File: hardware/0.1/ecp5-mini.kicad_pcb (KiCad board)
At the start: 4 copper layers, 52 x 27 mm, 109 parts, among them J1 Micro_SD_Card, J2 JTAG, J3 S7 Mini, J4 S7 Mini, J5 USB_C_Receptacle_USB2.0, Q1 BSS138, Q2 BSS138, Q3 BSS138, Q4 BSS138, SW1 SW_Push, U1 ECP5U_12_CABGA256, U2 TLV73325PDBV, U3 TLV62568DBV, U4 USBLC6-2SC6, U5 TLV62568DBV, U6 W25Q128JVSIQ, U7 S27KL0641

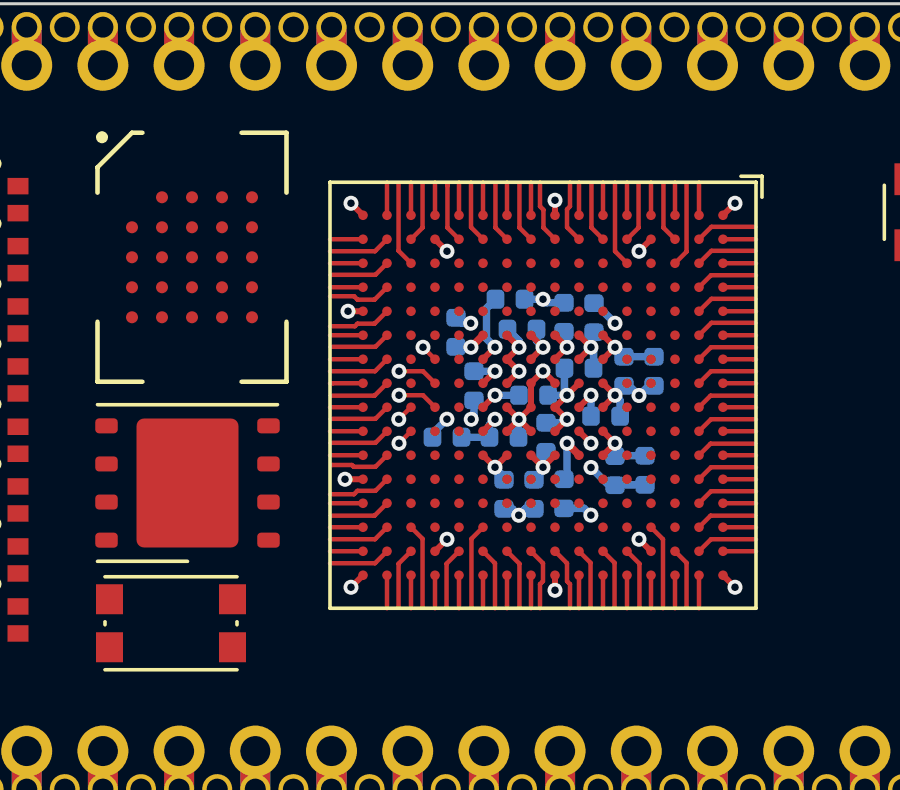
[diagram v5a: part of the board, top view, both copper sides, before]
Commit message: cleaning up schematic
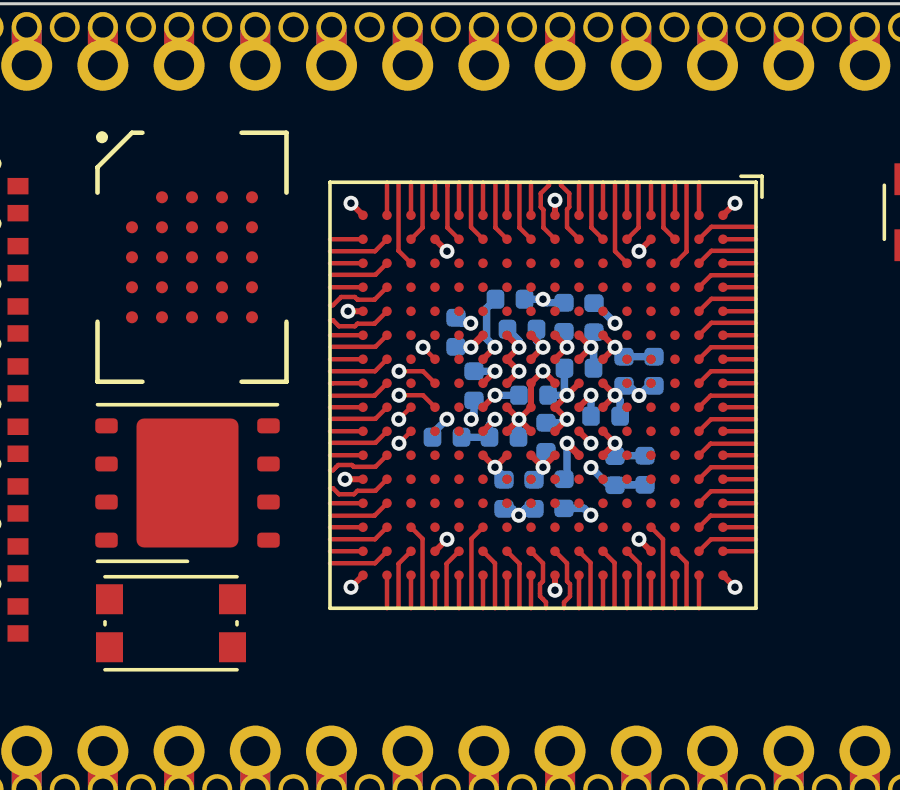
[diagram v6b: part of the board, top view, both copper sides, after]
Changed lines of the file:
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@@
   (segment (start 117.6 92.9) (end 117.115 92.9) (width 0.25) (layer "B.Cu") (net 100))
   (segment (start 118.4 96.9) (end 118.4 96.915) (width 0.25) (layer "B.Cu") (net 100))
-  (segment (start 113.628001 96.824999) (end 112.975001 96.824999) (width 0.15) (layer "F.Cu") (net 102))
+  (segment (start 113.175001 96.824999) (end 113.1 96.9) (width 0.15) (layer "F.Cu") (net 102))
   (segment (start 114.414999 96.885001) (end 113.688003 96.885001) (width 0.15) (layer "F.Cu") (net 102))
-  (segment (start 112.975001 96.824999) (end 112.924999 96.824999) (width 0.15) (layer "F.Cu") (net 102))
+  (segment (start 113.1 96.9) (end 113 97) (width 0.15) (layer "F.Cu") (net 102))
+  (segment (start 113 97) (end 112.9 97) (width 0.15) (layer "F.Cu") (net 102))
   (segment (start 114.8 96.5) (end 114.414999 96.885001) (width 0.15) (layer "F.Cu") (net 102))
   (segment (start 113.688003 96.885001) (end 113.628001 96.824999) (width 0.15) (layer "F.Cu") (net 102))
+  (segment (start 113.628001 96.824999) (end 113.175001 96.824999) (width 0.15) (layer "F.Cu") (net 102))
   (segment (start 114 95.7) (end 112.9 95.7) (width 0.15) (layer "F.Cu") (net 104))
   (segment (start 114.8 100.5) (end 114.8 101.6) (width 0.15) (layer "F.Cu") (net 106))
@@
   (segment (start 118.8 99.7) (end 119.214999 100.114999) (width 0.15) (layer "F.Cu") (net 124))
   (segment (start 119.214999 100.114999) (end 119.214999 101.585001) (width 0.15) (layer "F.Cu") (net 124))
+  (segment (start 120.1 101.4) (end 120.1 101.6) (width 0.15) (layer "F.Cu") (net 125))
+  (segment (start 120 101.3) (end 120.1 101.4) (width 0.15) (layer "F.Cu") (net 125))
   (segment (start 120 100.1) (end 120 100.696998) (width 0.15) (layer "F.Cu") (net 125))
+  (segment (start 119.9 101.2) (end 119.9 101.1) (width 0.15) (layer "F.Cu") (net 125))
   (segment (start 120 100.696998) (end 119.9 100.796998) (width 0.15) (layer "F.Cu") (net 125))
   (segment (start 119.6 99.7) (end 120 100.1) (width 0.15) (layer "F.Cu") (net 125))
-  (segment (start 119.9 100.796998) (end 119.9 101.6) (width 0.15) (layer "F.Cu") (net 125))
+  (segment (start 119.9 100.796998) (end 119.9 101.1) (width 0.15) (layer "F.Cu") (net 125))
+  (segment (start 120 101.3) (end 119.9 101.2) (width 0.15) (layer "F.Cu") (net 125))
+  (segment (start 120.9 100.796998) (end 120.9 101.1) (width 0.15) (layer "F.Cu") (net 126))
   (segment (start 120.8 100.1) (end 120.8 100.696998) (width 0.15) (layer "F.Cu") (net 126))
   (segment (start 120.4 99.7) (end 120.8 100.1) (width 0.15) (layer "F.Cu") (net 126))
+  (segment (start 120.7 101.403002) (end 120.7 101.6) (width 0.15) (layer "F.Cu") (net 126))
   (segment (start 120.8 100.696998) (end 120.9 100.796998) (width 0.15) (layer "F.Cu") (net 126))
-  (segment (start 120.9 100.796998) (end 120.9 101.6) (width 0.15) (layer "F.Cu") (net 126))
+  (segment (start 120.9 101.1) (end 120.9 101.203002) (width 0.15) (layer "F.Cu") (net 126))
+  (segment (start 120.9 101.203002) (end 120.7 101.403002) (width 0.15) (layer "F.Cu") (net 126))
   (segment (start 121.2 99.7) (end 121.585001 100.085001) (width 0.15) (layer "F.Cu") (net 127))
   (segment (start 121.585001 100.085001) (end 121.585001 101.585001) (width 0.15) (layer "F.Cu") (net 127))
@@
   (segment (start 125.6 97.7) (end 127.1 97.7) (width 0.15) (layer "F.Cu") (net 163))
   (segment (start 126 98.1) (end 127.1 98.1) (width 0.15) (layer "F.Cu") (net 164))
-  (segment (start 113.7 97.8) (end 112.9 97.8) (width 0.15) (layer "F.Cu") (net 165))
   (segment (start 114.8 97.3) (end 114.414999 97.685001) (width 0.15) (layer "F.Cu") (net 165))
+  (segment (start 113.7 97.8) (end 113.2 97.8) (width 0.15) (layer "F.Cu") (net 165))
+  (segment (start 113.2 97.8) (end 113 97.6) (width 0.15) (layer "F.Cu") (net 165))
   (segment (start 114.414999 97.685001) (end 113.814999 97.685001) (width 0.15) (layer "F.Cu") (net 165))
+  (segment (start 113 97.6) (end 112.9 97.6) (width 0.15) (layer "F.Cu") (net 165))
   (segment (start 113.814999 97.685001) (end 113.7 97.8) (width 0.15) (layer "F.Cu") (net 165))
   (segment (start 125.2 97.3) (end 125.6 96.9) (width 0.15) (layer "F.Cu") (net 178))
@@
   (segment (start 113 94.1) (end 112.9 94.1) (width 0.15) (layer "F.Cu") (net 228))
   (segment (start 114 94.1) (end 113 94.1) (width 0.15) (layer "F.Cu") (net 228))
+  (segment (start 113.2 92.2) (end 113 92) (width 0.15) (layer "F.Cu") (net 238))
   (segment (start 114.385001 92.114999) (end 113.815199 92.114999) (width 0.15) (layer "F.Cu") (net 238))
-  (segment (start 113.730198 92.2) (end 112.9 92.2) (width 0.15) (layer "F.Cu") (net 238))
+  (segment (start 113 92) (end 112.9 92) (width 0.15) (layer "F.Cu") (net 238))
+  (segment (start 113.730198 92.2) (end 113.2 92.2) (width 0.15) (layer "F.Cu") (net 238))
   (segment (start 113.815199 92.114999) (end 113.730198 92.2) (width 0.15) (layer "F.Cu") (net 238))
   (segment (start 114.8 91.7) (end 114.385001 92.114999) (width 0.15) (layer "F.Cu") (net 238))
   (segment (start 114 90.9) (end 112.9 90.9) (width 0.15) (layer "F.Cu") (net 248))
-  (segment (start 113.818001 91.314999) (end 113.703002 91.2) (width 0.15) (layer "F.Cu") (net 249))
-  (segment (start 113.703002 91.2) (end 112.9 91.2) (width 0.15) (layer "F.Cu") (net 249))
   (segment (start 114.8 90.9) (end 114.385001 91.314999) (width 0.15) (layer "F.Cu") (net 249))
+  (segment (start 113.271999 91.224999) (end 112.996998 91.5) (width 0.15) (layer "F.Cu") (net 249))
+  (segment (start 113.728001 91.224999) (end 113.271999 91.224999) (width 0.15) (layer "F.Cu") (net 249))
   (segment (start 114.385001 91.314999) (end 113.818001 91.314999) (width 0.15) (layer "F.Cu") (net 249))
+  (segment (start 113.818001 91.314999) (end 113.728001 91.224999) (width 0.15) (layer "F.Cu") (net 249))
+  (segment (start 112.996998 91.5) (end 112.9 91.5) (width 0.15) (layer "F.Cu") (net 249))
   (segment (start 114 90.1) (end 112.9 90.1) (width 0.15) (layer "F.Cu") (net 259))
   (segment (start 114.414999 90.485001) (end 112.914999 90.485001) (width 0.15) (layer "F.Cu") (net 260))
@@
   (segment (start 119.214999 88.914999) (end 119.214999 87.414999) (width 0.15) (layer "F.Cu") (net 279))
   (segment (start 119.6 89.3) (end 119.214999 88.914999) (width 0.15) (layer "F.Cu") (net 279))
-  (segment (start 119.9 88.203002) (end 119.9 87.4) (width 0.15) (layer "F.Cu") (net 280))
+  (segment (start 120.4 89.3) (end 120.014999 88.914999) (width 0.15) (layer "F.Cu") (net 280))
+  (segment (start 120.2 87.496998) (end 120.2 87.4) (width 0.15) (layer "F.Cu") (net 280))
   (segment (start 120.014999 88.914999) (end 120.014999 88.318001) (width 0.15) (layer "F.Cu") (net 280))
-  (segment (start 120.014999 88.318001) (end 119.9 88.203002) (width 0.15) (layer "F.Cu") (net 280))
-  (segment (start 120.4 89.3) (end 120.014999 88.914999) (width 0.15) (layer "F.Cu") (net 280))
-  (segment (start 120.8 88.303002) (end 120.9 88.203002) (width 0.15) (layer "F.Cu") (net 281))
+  (segment (start 119.924999 87.771999) (end 120.2 87.496998) (width 0.15) (layer "F.Cu") (net 280))
+  (segment (start 120.014999 88.318001) (end 119.924999 88.228001) (width 0.15) (layer "F.Cu") (net 280))
+  (segment (start 119.924999 88.228001) (end 119.924999 87.771999) (width 0.15) (layer "F.Cu") (net 280))
+  (segment (start 120.875001 88.228001) (end 120.875001 87.771999) (width 0.15) (layer "F.Cu") (net 281))
+  (segment (start 120.875001 87.771999) (end 120.6 87.496998) (width 0.15) (layer "F.Cu") (net 281))
   (segment (start 120.8 88.9) (end 120.8 88.303002) (width 0.15) (layer "F.Cu") (net 281))
+  (segment (start 120.6 87.496998) (end 120.6 87.4) (width 0.15) (layer "F.Cu") (net 281))
   (segment (start 121.2 89.3) (end 120.8 88.9) (width 0.15) (layer "F.Cu") (net 281))
-  (segment (start 120.9 88.203002) (end 120.9 87.4) (width 0.15) (layer "F.Cu") (net 281))
+  (segment (start 120.8 88.303002) (end 120.875001 88.228001) (width 0.15) (layer "F.Cu") (net 281))
   (segment (start 122 89.3) (end 121.614999 88.914999) (width 0.15) (layer "F.Cu") (net 282))
   (segment (start 121.614999 88.914999) (end 121.614999 87.414999) (width 0.15) (layer "F.Cu") (net 282))

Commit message: layout ++
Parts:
- removed R23, R24, R26, R27, R29, R31, R32, R33: 220R, Resistor_SMD:R_0402_1005Metric
- added C14: 100n, Capacitor_SMD:C_0402_1005Metric, F.Cu at (134.6, 94.0)
- added RN2: 220R, Resistor_SMD:R_Array_Convex_4x0402, B.Cu at (65.9, 102.2)
- added RN3: 220R, Resistor_SMD:R_Array_Convex_4x0402, B.Cu at (65.9, 105.2)
- added X1: DSC6101CI2A-016, josh-oscillators:CDFN_3.2x2.5mm_XO, F.Cu at (132.2, 93.6)
- C13, C15, C18, Q2, Q3, Q4, R12, R13, R14, R15, R16, R17, R18, R19, R21, R22, R25, R28, R30, R34, R5, R8: moved to B.Cu
- R20: value 51R -> 22R; moved to B.Cu
- RN1: value 10k -> 10K; moved to B.Cu
- moved R14 32.5 mm to (116.2, 98.7), turned to 90 degrees
- moved R16 30.3 mm to (115.1, 98.7), turned to 90 degrees
- moved R13 30.2 mm to (116.2, 99.7), turned to 90 degrees
- moved R17 29.5 mm to (114.0, 99.7), turned to 90 degrees
- moved R18 28.9 mm to (114.0, 98.7), turned to 90 degrees
- moved R15 28.6 mm to (115.1, 99.7), turned to 90 degrees
- moved R20 26.2 mm to (115.5, 94.9), turned to 0 degrees
- moved R9 23.6 mm to (136.3, 94.5), turned to 0 degrees
- moved R10 21.9 mm to (136.3, 95.5), turned to 180 degrees
- moved R22 21.4 mm to (146.1, 86.2), turned to 180 degrees
- moved R34 20.6 mm to (146.1, 87.4), turned to 0 degrees
- moved R11 20.2 mm to (136.3, 96.5), turned to 180 degrees
- moved RN1 20.1 mm to (107.5, 96.4)
- moved R19 18.0 mm to (109.6, 93.3)
- moved C45 17.7 mm to (109.6, 91.2), turned to 0 degrees
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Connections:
- net /Board IO/PORT_A0 renamed /PORT_A0
- net /Board IO/PORT_A1 renamed /PORT_A1
- net /Board IO/PORT_A2 renamed /PORT_A2
- net /Board IO/PORT_A3 renamed /PORT_A3
- net /Board IO/PORT_A4 renamed /PORT_A4
- net /Board IO/PORT_A5 renamed /PORT_A5
- net /Board IO/PORT_A6 renamed /PORT_A6
- net /Board IO/PORT_A7 renamed /PORT_A7
- net /Board IO/PORT_B0 renamed /PORT_B0
- net /Board IO/PORT_B1 renamed /PORT_B1
- net /Board IO/PORT_B2 renamed /PORT_B2
- net /Board IO/PORT_B3 renamed /PORT_B3
- net /Board IO/PORT_B4 renamed /PORT_B4
- net /Board IO/PORT_B5 renamed /PORT_B5
- net /Board IO/PORT_B6 renamed /PORT_B6
- net /Board IO/PORT_B7 renamed /PORT_B7
- net /Board IO/PORT_C0 renamed /PORT_C0
- net /Board IO/PORT_C1 renamed /PORT_C1
- net /Board IO/PORT_C2 renamed /PORT_C2
- net /Board IO/PORT_C3 renamed /PORT_C3
- net /Board IO/PORT_C4 renamed /PORT_C4
- net /Board IO/PORT_C5 renamed /PORT_C5
- net /Board IO/PORT_C6 renamed /PORT_C6
- net /Board IO/PORT_C7 renamed /PORT_C7
- net /Board IO/PORT_D0 renamed /PORT_D0
- net /Board IO/PORT_D1 renamed /PORT_D1
- net /Board IO/PORT_D2 renamed /PORT_D2
- net /Board IO/PORT_D3 renamed /PORT_D3
- net /Board IO/PORT_D4 renamed /PORT_D4
- net /Board IO/PORT_D5 renamed /PORT_D5
- net /Board IO/PORT_D6 renamed /PORT_D6
- net /Board IO/PORT_D7 renamed /PORT_D7
- net /Board IO/PORT_E0 renamed /PORT_E0
- net /Board IO/PORT_E1 renamed /PORT_E1
- net /Board IO/PORT_E2 renamed /PORT_E2
- net /Board IO/PORT_E3 renamed /PORT_E3
- net /Board IO/PORT_E4 renamed /PORT_E4
- net /Board IO/PORT_E5 renamed /PORT_E5
- net /Board IO/PORT_E6 renamed /PORT_E6
- net /Board IO/PORT_E7 renamed /PORT_E7
- net /Board IO/PORT_F0 renamed /PORT_F0
- net /Board IO/PORT_F1 renamed /PORT_F1
- net /Board IO/PORT_F2 renamed /PORT_F2
- net /Board IO/PORT_F3 renamed /PORT_F3
- net /Board IO/PORT_F4 renamed /PORT_F4
- net /Board IO/PORT_F5 renamed /PORT_F5
- net /Board IO/PORT_F6 renamed /PORT_F6
- net /Board IO/PORT_F7 renamed /PORT_F7
- net /Board IO/PORT_G0 renamed /PORT_G0
- net /Board IO/PORT_G1 renamed /PORT_G1
- net /Board IO/PORT_G2 renamed /PORT_G2
- net /Board IO/PORT_G3 renamed /PORT_G3
- net /Board IO/PORT_G4 renamed /PORT_G4
- net /Board IO/PORT_G5 renamed /PORT_G5
- net /Board IO/PORT_G6 renamed /PORT_G6
- net /Board IO/PORT_G7 renamed /PORT_G7
- net /FPGA Config/USB_D+ renamed /USB_D+
- net /FPGA Config/USB_D- renamed /USB_D-
- net /FPGA Config/USB_PU renamed /USB_PU
- net /Hyperram / Micro SD/SD.CMD renamed /SD_CMD
- net /Hyperram / Micro SD/SD.DAT0 renamed /SD_DAT0
- net /Hyperram / Micro SD/SD.DAT1 renamed /SD_DAT1
- net /Hyperram / Micro SD/SD.DAT2 renamed /SD_DAT2
- net /Hyperram / Micro SD/SD.DAT3 renamed /SD_DAT3
- net /Hyperram / Micro SD/SD.DETA renamed /SD_DETA
- net /Hyperram / Micro SD/SD.DETB renamed /SD_DETB
- J1 pad 5: +3V3 -> /SD_CLK
- RN1 pad 2: /FPGA Config/CFG.CLK -> /FPGA Config/CFG.IO1
- U1 pad A7: Net-(U1-PadA7) -> /CLK_16MHZ
- U1 pad N3: Net-(U1-PadN3) -> /HR_nCS
- U1 pad P1: Net-(U1-PadP1) -> /HR_CK_P
- U1 pad P2: Net-(U1-PadP2) -> /HR_CK_N
- U1 pad P3: Net-(U1-PadP3) -> /HR_DQ4
- U1 pad P5: Net-(U1-PadP5) -> /HR_DQ7
- U1 pad R1: Net-(U1-PadR1) -> /HR_nRST
- U1 pad R2: Net-(U1-PadR2) -> /HR_RWDS
- U1 pad R3: Net-(U1-PadR3) -> /HR_DQ2
- U1 pad R4: Net-(U1-PadR4) -> /HR_DQ1
- U1 pad R5: Net-(U1-PadR5) -> /HR_DQ6
- U1 pad R7: Net-(U1-PadR7) -> /FPGA Config/LED_USR
- U1 pad T2: Net-(U1-PadT2) -> /HR_DQ0
- U1 pad T3: Net-(U1-PadT3) -> /HR_DQ3
- U1 pad T4: Net-(U1-PadT4) -> /HR_DQ5
- U1 pad T6: /FPGA Config/LED_USR -> Net-(U1-PadT6)
- U7 pad A3: /Hyperram / Micro SD/nCS -> /HR_nCS
- U7 pad A4: /Hyperram / Micro SD/nRST -> /HR_nRST
- U7 pad B1: /Hyperram / Micro SD/nCK -> /HR_CK_N
- U7 pad B2: /Hyperram / Micro SD/CK -> /HR_CK_P
- U7 pad C3: /Hyperram / Micro SD/RWDS -> /HR_RWDS
- U7 pad C4: /Hyperram / Micro SD/DQ2 -> /HR_DQ2
- U7 pad D2: /Hyperram / Micro SD/DQ1 -> /HR_DQ1
- U7 pad D3: /Hyperram / Micro SD/DQ0 -> /HR_DQ0
- U7 pad D4: /Hyperram / Micro SD/DQ3 -> /HR_DQ3
- U7 pad D5: /Hyperram / Micro SD/DQ4 -> /HR_DQ4
- U7 pad E1: /Hyperram / Micro SD/DQ7 -> /HR_DQ7
- U7 pad E2: /Hyperram / Micro SD/DQ6 -> /HR_DQ6
- U7 pad E3: /Hyperram / Micro SD/DQ5 -> /HR_DQ5
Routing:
- net /LEDs/CAT_B: track 0.00 -> 19.5 mm
- net /LEDs/CAT_R: track 0.00 -> 19.2 mm
- net /LEDs/CAT_G: track 0.00 -> 18.7 mm
- net /HR_CK_N: track 0.00 -> 16.6 mm
- net /FPGA Config/CFG.IO2: track 0.00 -> 15.0 mm, vias 0 -> 2
- net /FPGA Config/CFG.CLK: track 1.37 -> 16.0 mm, vias 1 -> 2
- net /FPGA Config/CFG.IO0: track 1.10 -> 14.5 mm
- net /FPGA Config/CFG.IO3: track 0.57 -> 13.5 mm, vias 1 -> 2
- net /HR_DQ7: track 0.00 -> 12.5 mm
- net /HR_CK_P: track 0.00 -> 11.8 mm
- net /HR_nCS: track 0.00 -> 11.7 mm
- net +3V3: track 13.2 -> 23.4 mm, vias 7 -> 11
- net GND: track 33.7 -> 43.7 mm, vias 31 -> 38
- net /HR_DQ6: track 0.00 -> 9.95 mm
- net /FPGA Config/nBTN_USR: track 2.06 -> 11.6 mm
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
